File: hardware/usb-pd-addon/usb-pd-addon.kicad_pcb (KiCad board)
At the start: 2 copper layers, 48 x 40 mm, 54 parts, among them J1 Conn_02x10_Odd_Even, J2 Conn_02x10_Odd_Even, J3 USB_TYPE_C, J4 Conn_02x05_Odd_Even, J5 Conn_02x05_Odd_Even, J6 EXT, J7 TP1, J8 TP2, J9 TP3, U1 FUSB302B, U2 AP2171W, U3 SN74AVC1T45DBVR, U4 SN74AVC1T45DBVR, U5 SN74AVC1T45DBVR, U6 SN74AVC1T45DBVR, U7 AP2127K-ADJ, U8 AP2127K-ADJ

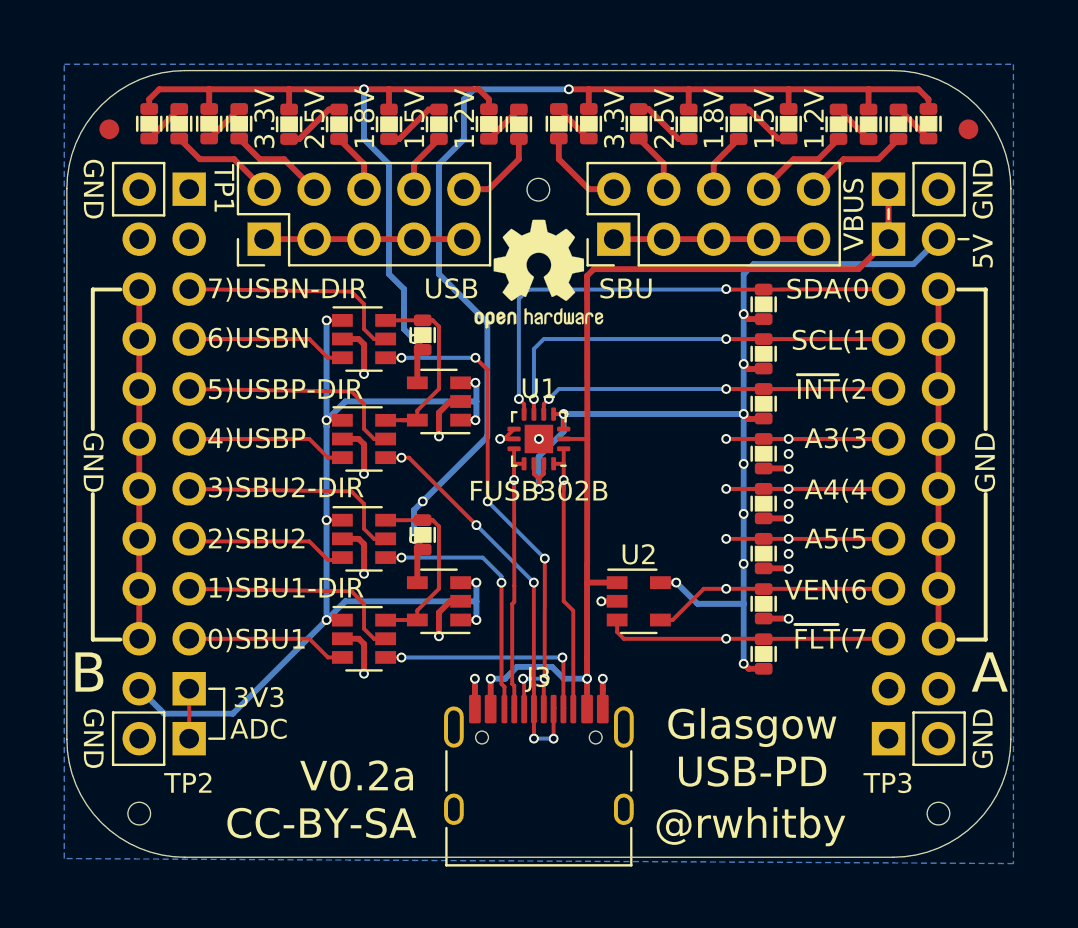
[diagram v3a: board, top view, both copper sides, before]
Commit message: Added bypass caps.
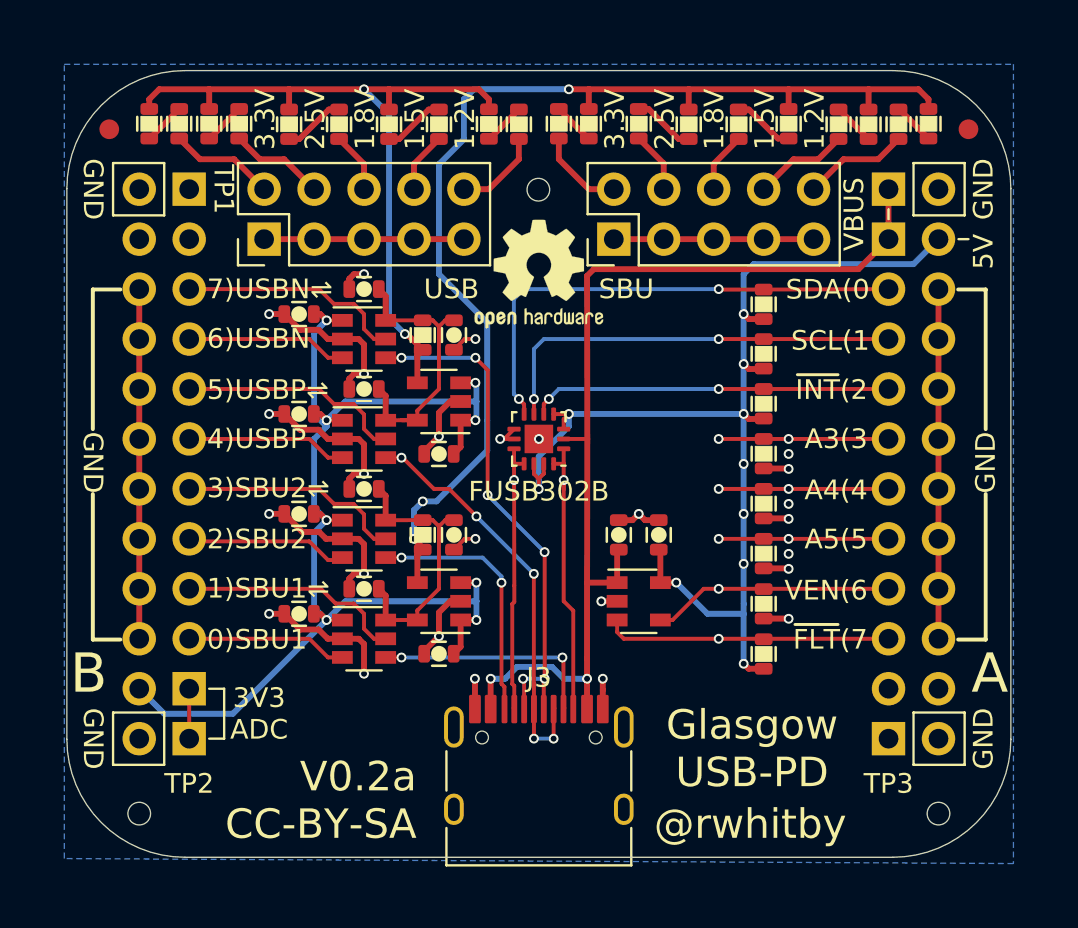
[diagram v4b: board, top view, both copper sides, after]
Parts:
- added C1: 0.1u, pkl_dipol:C_0603, F.Cu at (43.7, 44.5)
- added C10: 0.1u, pkl_dipol:C_0603, F.Cu at (43.7, 59.7)
- added C11: 0.1u, pkl_dipol:C_0603, F.Cu at (47.0, 48.3)
- added C12: 0.1u, pkl_dipol:C_0603, F.Cu at (47.0, 58.4)
- added C13: 1uF, pkl_dipol:C_0603, F.Cu at (62.0, 55.7)
- added C14: 1uF, pkl_dipol:C_0603, F.Cu at (59.9, 55.7)
- added C2: 0.1u, pkl_dipol:C_0603, F.Cu at (43.7, 54.6)
- added C3: 0.1u, pkl_dipol:C_0603, F.Cu at (47.0, 43.2)
- added C4: 0.1u, pkl_dipol:C_0603, F.Cu at (47.0, 53.3)
- added C5: 1uF, pkl_dipol:C_0603, F.Cu at (50.8, 51.6)
- added C6: 1uF, pkl_dipol:C_0603, F.Cu at (50.8, 61.7)
- added C7: 1uF, pkl_dipol:C_0603, F.Cu at (51.6, 45.5)
- added C8: 1uF, pkl_dipol:C_0603, F.Cu at (51.6, 55.7)
- added C9: 0.1u, pkl_dipol:C_0603, F.Cu at (43.7, 49.5)
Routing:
- net GND: track 78.6 -> 108.5 mm, vias 15 -> 23
- net +3V3: track 53.9 -> 62.3 mm
- net /VIO_USB: track 10.5 -> 14.8 mm
- net /VIO_SBU: track 10.5 -> 14.8 mm
- net +5V: track 56.6 -> 58.8 mm
- net /VBUS: track 50.4 -> 52.1 mm
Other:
- board text added: "1)SBU1⇌"
- board text added: "3)SBU2⇌"
- board text added: "5)USBP⇌"
- board text added: "7)USBN⇌"
- board text added: "SBU1⇌(1"
- board text added: "SBU2⇌(3"
- board text added: "USBN⇌(7"
- board text added: "USBP⇌(5"
- board text removed: "1)SBU1-DIR"
- board text removed: "3)SBU2-DIR"
- board text removed: "5)USBP-DIR"
- board text removed: "7)USBN-DIR"
- board text removed: "SBU1-DIR(1"
- board text removed: "SBU2-DIR(3"
- board text removed: "USBN-DIR(7"
- board text removed: "USBP-DIR(5"

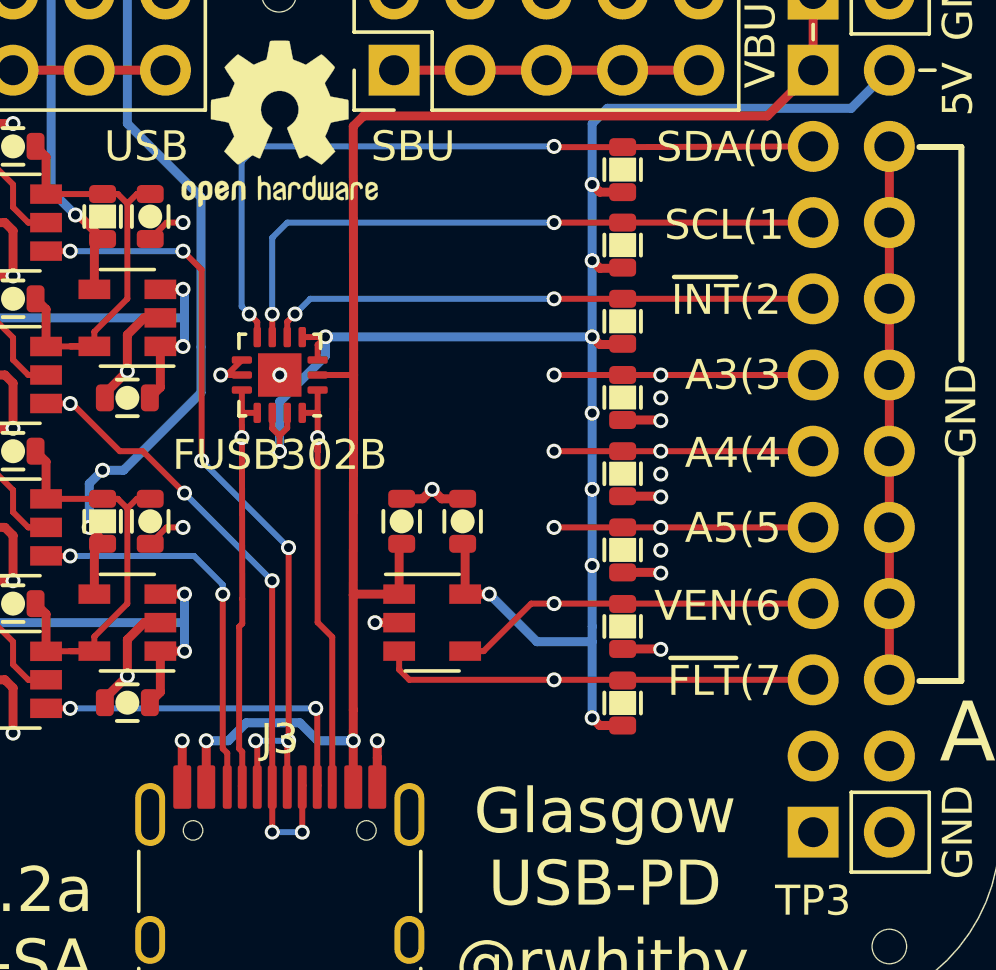
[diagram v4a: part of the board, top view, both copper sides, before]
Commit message: Corrected D+ pullup circuitry and added bypass cap.
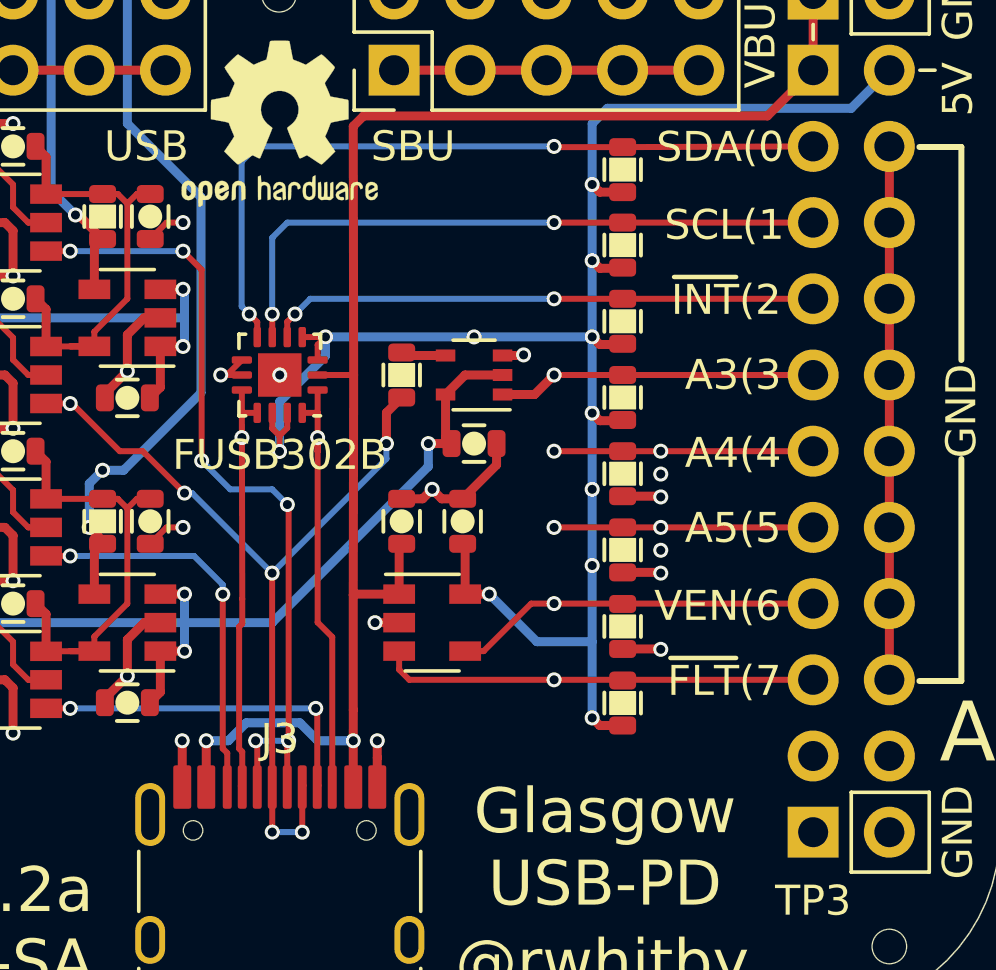
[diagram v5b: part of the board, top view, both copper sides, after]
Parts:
- added C15: 0.1u, pkl_dipol:C_0603, F.Cu at (62.4, 53.1)
- added R31: 1K5, pkl_dipol:R_0603, F.Cu at (59.9, 50.8)
- added U9: NC7SZ125P5X, Package_TO_SOT_SMD:SOT-353_SC-70-5, F.Cu at (62.4, 50.8)
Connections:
- net /A3 renamed /~FSEN
- net /FLT_N renamed /~FLT
- net /INT_N renamed /~INT
- R4 pad 1: Net-(R4-Pad1) -> +5V
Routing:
- net +3V3: track 62.3 -> 78.0 mm, vias 8 -> 9
- net /USBP: track 21.0 -> 28.8 mm, vias 5 -> 6
- net GND: track 108.5 -> 111.5 mm
- net /~FSEN: track 8.64 -> 10.6 mm, vias 2 -> 1
- net Net-(R31-Pad2): track 0.00 -> 1.50 mm
- net Net-(R4-Pad1): track 1.28 -> 0.00 mm, vias 1 -> 0
- net +5V: track 58.8 -> 59.9 mm, vias 10 -> 11
- net /USBN: track 26.7 -> 27.5 mm

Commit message: Better mnemonic for the FS pull-up switch enable.
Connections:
- net /~FSEN renamed /~FSPU
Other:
- board text added: "3)~FS"
- board text added: "~FS ~(3"
- board text removed: "3)A3"
- board text removed: "A3(3"

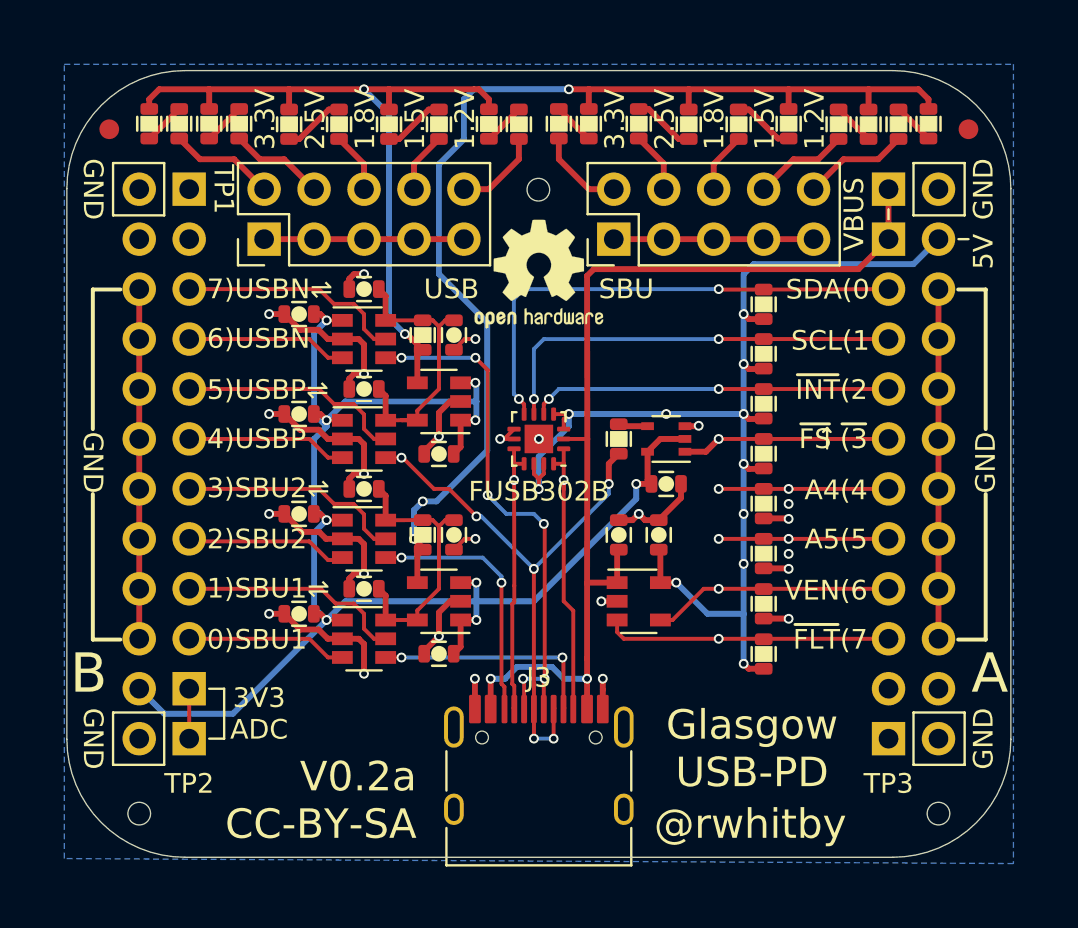
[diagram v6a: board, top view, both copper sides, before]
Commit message: Added LEDs and a README.
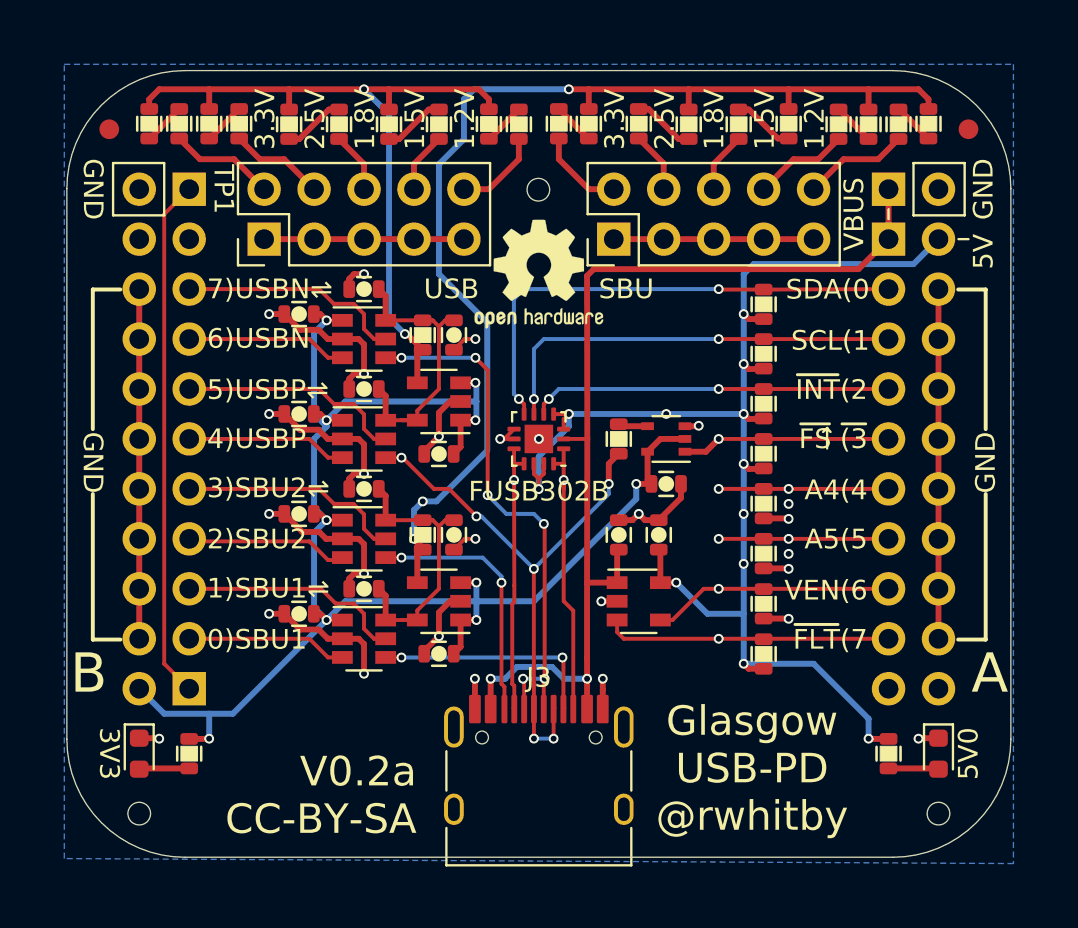
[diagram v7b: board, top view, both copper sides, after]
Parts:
- removed J8: TP2, Connector_PinHeader_2.54mm:PinHeader_1x02_P2.54mm_Vertical
- removed J9: TP3, Connector_PinHeader_2.54mm:PinHeader_1x02_P2.54mm_Vertical
- added D1: GRN, LED_SMD:LED_0603_1608Metric, F.Cu at (35.6, 66.8)
- added D2: GRN, LED_SMD:LED_0603_1608Metric, F.Cu at (76.2, 66.8)
- added R32: 20K, pkl_dipol:R_0603, F.Cu at (38.1, 66.8)
- added R33: 20K, pkl_dipol:R_0603, F.Cu at (73.7, 66.8)
- J6: value EXT -> TPAS
- J7: value TP1 -> TPBS
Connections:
- J7 pad 1: Net-(J7-Pad1) -> /BS
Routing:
- net /BS: track 2.54 -> 26.5 mm
- net +5V: track 59.9 -> 69.4 mm, vias 11 -> 12
- net Net-(D2-Pad2): track 0.00 -> 2.56 mm
- net Net-(D1-Pad2): track 0.00 -> 2.56 mm
- net +3V3: track 78.0 -> 80.3 mm, vias 9 -> 10
- net GND: track 111.5 -> 113.5 mm, vias 23 -> 25
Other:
- board text added: "3V3"
- board text added: "5V0"
- board text added: "Glasgow USB-PD @rwhitby"
- board text removed: "3V3 ADC"
- board text removed: "@rwhitby"
- board text removed: "Glasgow USB-PD"
- board text removed: "TP2"
- board text removed: "TP3"

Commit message: Changed 5V LED resistor to 51K
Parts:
- R33: value 20K -> 51K
